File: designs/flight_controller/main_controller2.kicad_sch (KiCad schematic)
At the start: 74 parts, among them J1 xt30, J10 Conn_01x15, J3 xt30, J4 Conn_01x02, J6 Conn_01x02, J7 Conn_01x02, J8 Conn_01x02, J9 Conn_01x16, Q1 FDN359BN, SW1 SW_SPST, SW2 SW_SPST, U1 ESP32-PICO-D4, U10 BTN7030-1EPA, U11 PCA9557PW, U12 INA219AxD, U13 W25N02KVZEIR, U14 MCP2517FD-xSL, U15 SN65HVD230, U2 BMI088, U3 china_buck_converter, U4 AP7361-33ER-13, U5 MS5611-01BA, U6 BTS70802, U7 BTN7030-1EPA, U8 BTN7030-1EPA, U9 BTN7030-1EPA, Y1 40MHz

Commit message: fix grid
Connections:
- net PYRO_1_EN is gone; now on net PYRO_1: U7.6 (IN)
- net PYRO_2_EN is gone; now on net PYRO_2: U9.6 (IN)
- net PYRO_3_EN is gone; now on net PYRO_3: U8.6 (IN)
- net PYRO_4_EN is gone; now on net PYRO_4: U10.6 (IN)
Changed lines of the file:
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@@
   (no_connect (at 388.62 43.18))
   (no_connect (at 115.57 158.75))
-  (no_connect (at 130.6576 50.9016))
+  (no_connect (at 130.81 50.8))
   (no_connect (at 322.58 226.06))
   (no_connect (at 322.58 228.6))
@@
   (no_connect (at 322.58 218.44))
   (no_connect (at 243.84 151.13))
-  (no_connect (at 130.9624 48.3108))
+  (no_connect (at 130.81 48.26))
   (no_connect (at 213.995 90.17))
   (no_connect (at 213.995 82.55))
   (no_connect (at 243.84 158.75))
   (no_connect (at 64.77 234.95))
-  (no_connect (at 130.6576 45.9232))
+  (no_connect (at 130.81 45.72))
   (no_connect (at 370.84 80.01))
   (no_connect (at 353.06 38.1))
@@
     (effects (font (size 1.27 1.27)) (justify left bottom))
   )
-  (label "PYRO_3_EN" (at 74.93 262.89 180)
+  (label "PYRO_3" (at 74.93 262.89 180)
     (effects (font (size 1.27 1.27)) (justify right bottom))
   )
@@
     (effects (font (size 1.27 1.27)) (justify right bottom))
   )
-  (label "PYRO_1_EN" (at 74.93 232.41 180)
+  (label "PYRO_1" (at 74.93 232.41 180)
     (effects (font (size 1.27 1.27)) (justify right bottom))
   )
@@
     (effects (font (size 1.27 1.27)) (justify left bottom))
   )
-  (label "PYRO_4_EN" (at 139.7 264.16 180)
+  (label "PYRO_4" (at 139.7 264.16 180)
     (effects (font (size 1.27 1.27)) (justify right bottom))
   )
@@
     (effects (font (size 1.27 1.27)) (justify right bottom))
   )
-  (label "PYRO_2_EN" (at 139.7 232.41 180)
-    (effects (font (size 1.27 1.27)) (justify right bottom))
-  )
+  (label "PYRO_2" (at 139.7 232.41 180)
+    (effects (font (size 1.27 1.27)) (justify right bottom))
+  )

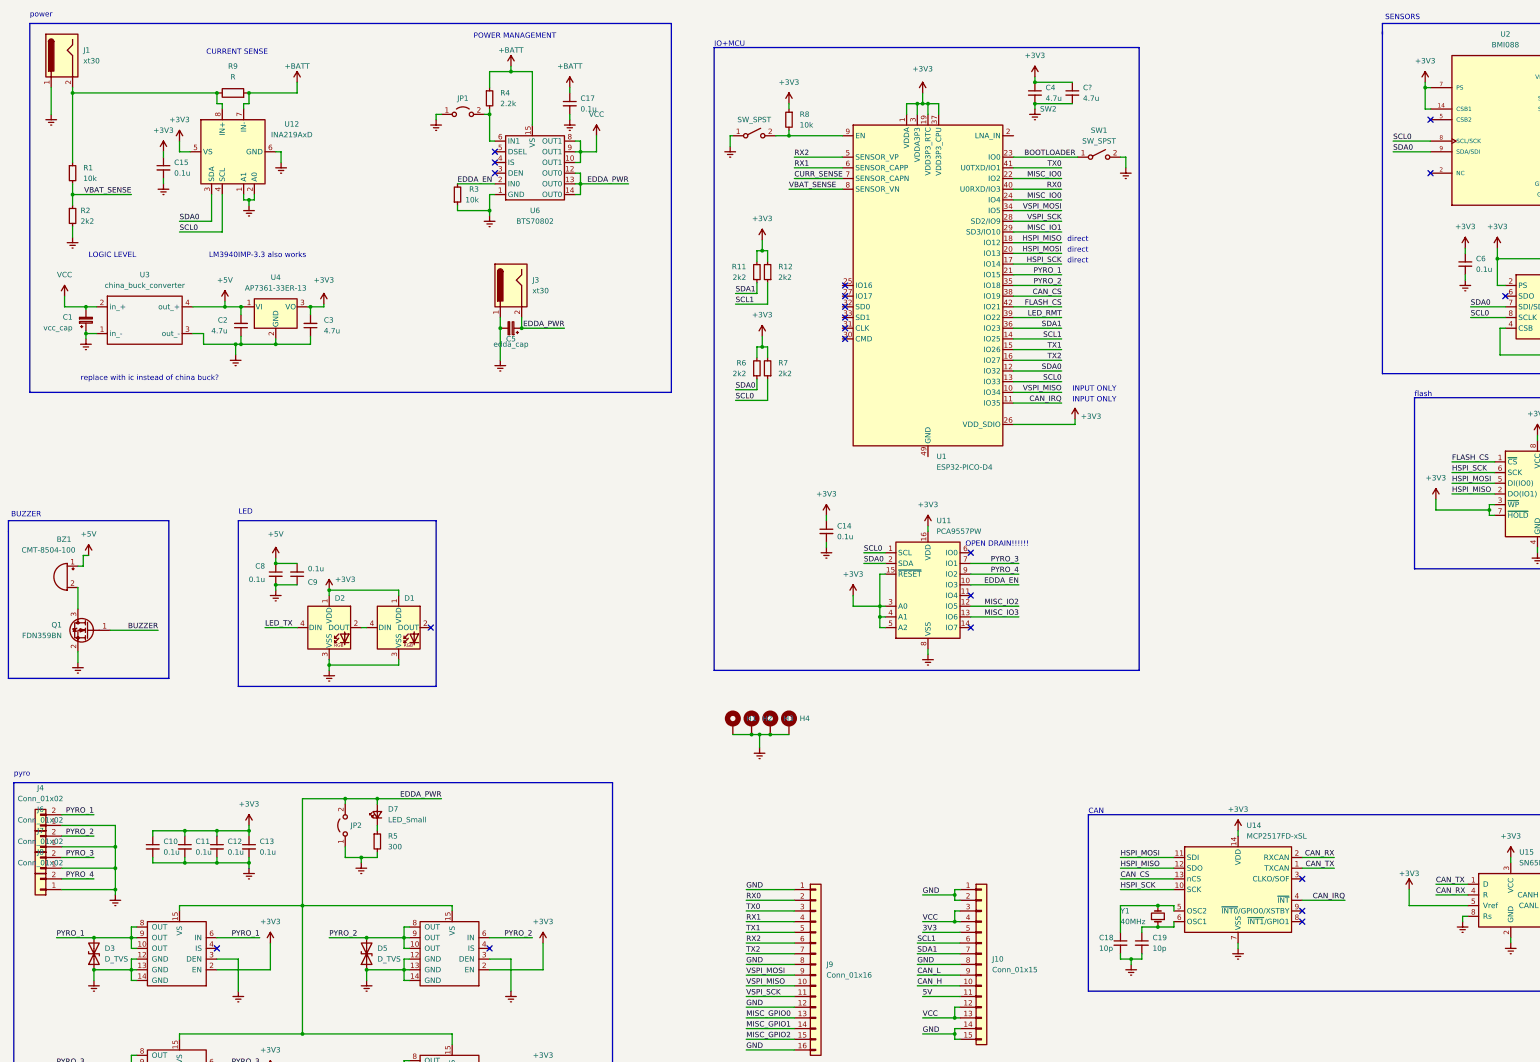
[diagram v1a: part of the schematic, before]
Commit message: preliminary layout
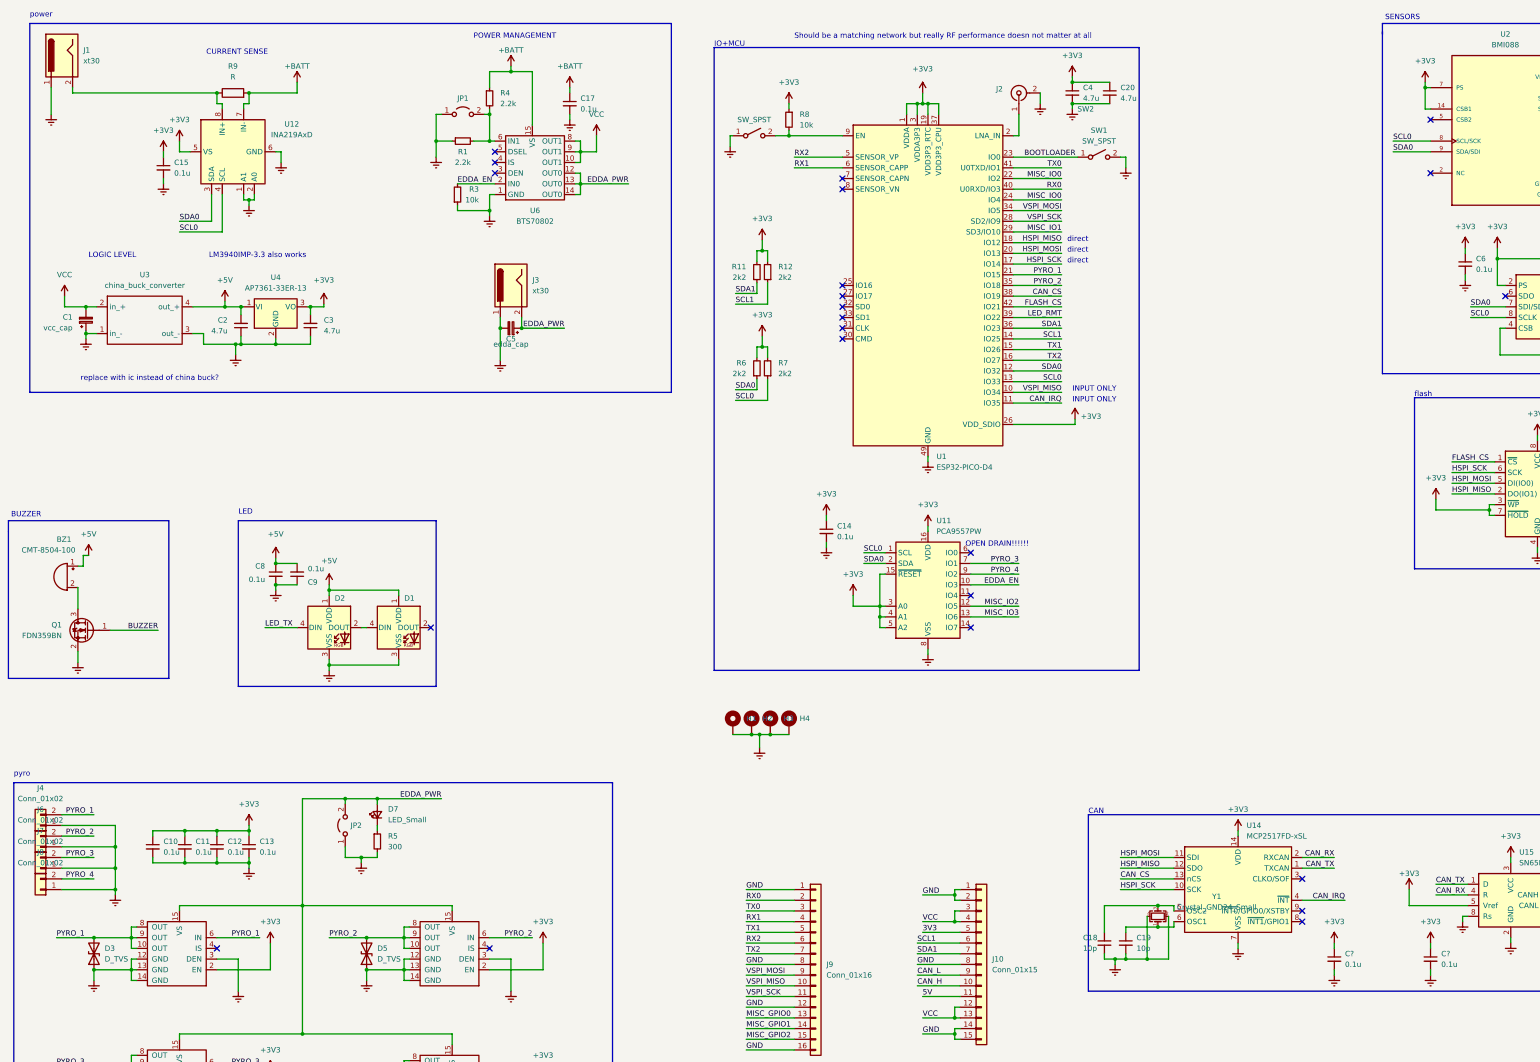
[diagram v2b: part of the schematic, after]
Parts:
- removed R2: 2k2, Resistor_SMD:R_0603_1608Metric, symbol Device:R_Small
- removed Y1: 40MHz, Oscillator:Oscillator_SMD_SeikoEpson_SG8002CE-4Pin_3.2x2.5mm_HandSoldering, symbol Device:Crystal_Small
- added C? (x2): 0.1u, Capacitor_SMD:C_0603_1608Metric, symbol Device:C_Small
- added J2: Conn_Coaxial, Connector_Coaxial:U.FL_Molex_MCRF_73412-0110_Vertical, symbol Connector:Conn_Coaxial
- added Y1: Crystal_GND24_Small, lib:CX3225SB40000D0FLJCC, symbol Device:Crystal_GND24_Small
- R1: value 10k -> 2.2k
- gave numbers to parts that had none: 1
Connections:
- net +3V3: now also C?.1, C?.1; no longer D1.1 (VDD), D2.1 (VDD)
- net +5V: now also D1.1 (VDD), D2.1 (VDD)
- net Earth: now also R1.1, U1.49 (GND), C?.2, C?.2, J2.2 (Ext), Y1.2, Y1.4
- net at JP1.2 (B), R4.2, U6.6 (IN1): now also R1.2
- net at J1.2, R9.1, U12.8 (IN+): no longer R1.1
- net at C18.1, U14.5 (OSC2): now also Y1.3
- net at C19.1, U14.6 (OSC1): now also Y1.1
- net at U1.2 (LNA_IN): now also J2.1 (In)
- net CURR_SENSE: no longer names the net of U1.7 (SENSOR_CAPN)
- net VBAT_SENSE: no longer names the net of U1.8 (SENSOR_VN)
- net VBAT_SENSE: no longer R1.2
- no-connect marks 25 -> 27
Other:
- note added: "Should be a matching network but really RF performance doesn not matter at all"
- moved on the sheet: C18, C19, C20, C4

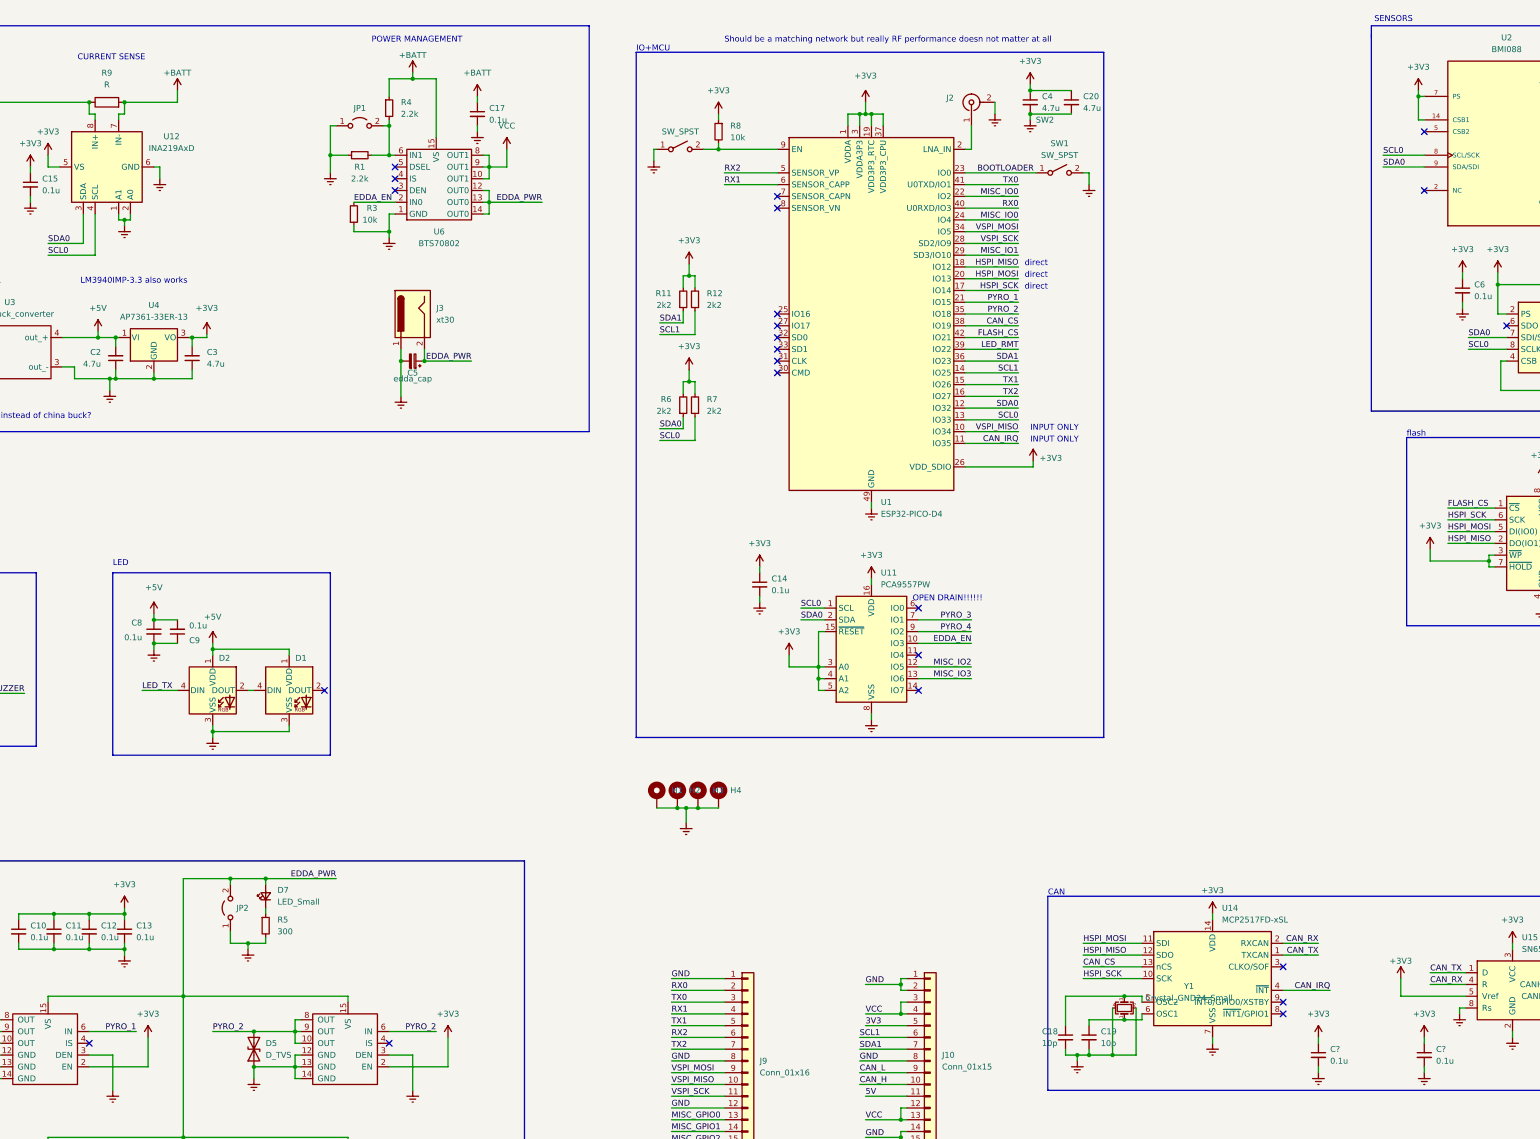
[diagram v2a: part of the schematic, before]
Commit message: add ufl
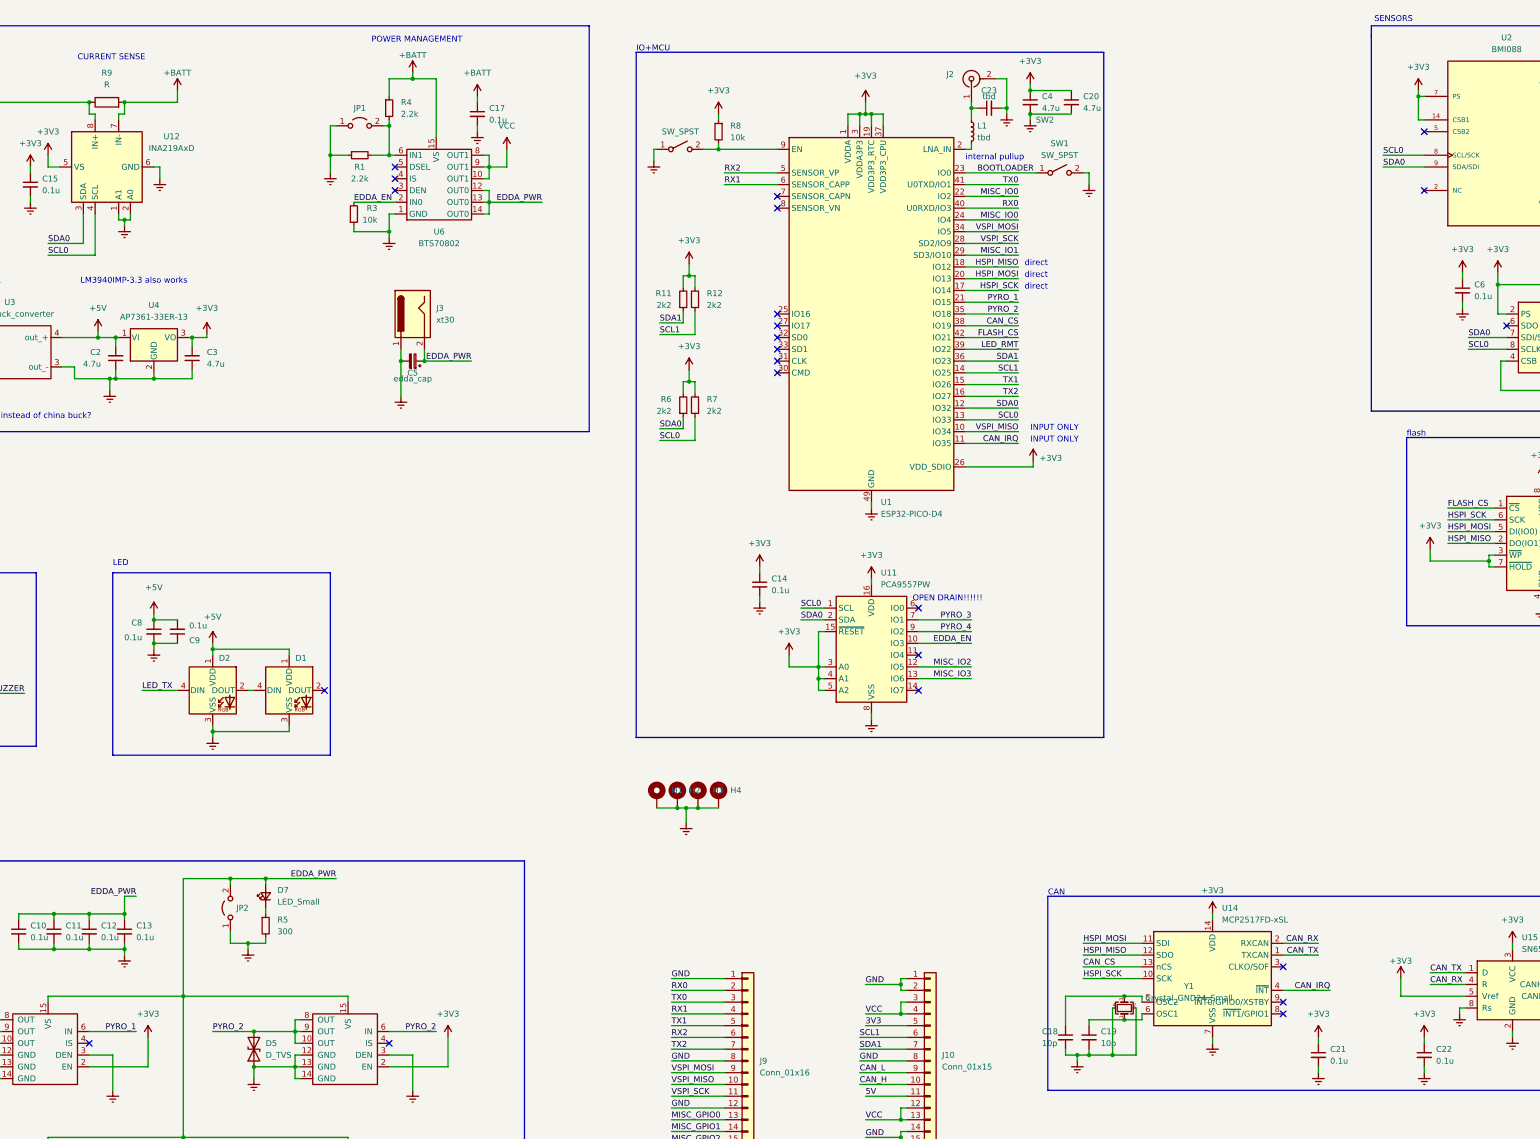
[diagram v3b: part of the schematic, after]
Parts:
- added C23: tbd, Capacitor_SMD:C_0603_1608Metric, symbol Device:C_Small
- added L1: tbd, Inductor_SMD:L_0603_1608Metric, symbol Device:L_Small
- gave numbers to parts that had none: 2
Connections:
- net +3V3: no longer C10.1, C11.1, C12.1, C13.1
- net EDDA_PWR: now also C10.1, C11.1, C12.1, C13.1
- net Earth: now also C23.2
- net at J2.1 (In): now also C23.1, L1.1; no longer U1.2 (LNA_IN)
- new net: L1.2, U1.2 (LNA_IN)
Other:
- note added: "internal pullup"
- note removed: "Should be a matching network but really RF performance doesn not matter at all"
- moved on the sheet: J2

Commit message: routing done
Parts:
- added F1: Fuse_Small, Fuse:Fuse_1812_4532Metric_Pad1.30x3.40mm_HandSolder, symbol Device:Fuse_Small
- added R13: 10k, Resistor_SMD:R_0603_1608Metric, symbol Device:R_Small
- added R14, R2: 2k2, Resistor_SMD:R_0603_1608Metric, symbol Device:R_Small
- R4: value 2.2k -> 4k7
- Y1: value Crystal_GND24_Small -> CX3225SB40000D0FLJCC
- renumbered D2 to D1, D1 to D2
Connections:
- net 3V3 is gone; now on net +5V: J10.5 (Pin_5)
- net 5V is gone; now on net +3V3: J10.11 (Pin_11)
- net LED_TX is gone; now on net LED_RMT: D1.4 (DIN)
- net MISC_GPIO0 is gone; now on net MISC_IO0: J9.13 (Pin_13)
- net MISC_GPIO1 is gone; now on net MISC_IO1: J9.14 (Pin_14)
- net MISC_GPIO2 is gone; now on net MISC_IO2: J9.15 (Pin_15)
- net +BATT: now also R2.1
- net BUZZER: now also U1.24 (IO4)
- net EDDA_PWR: now also J10.12 (Pin_12), J10.13 (Pin_13), J10.3 (Pin_3), J10.4 (Pin_4), F1.2, R13.1, R2.2; no longer U6.12 (OUT0), U6.13 (OUT0), U6.14 (OUT0)
- net Earth: now also J10.1 (Pin_1), J10.14 (Pin_14), J10.15 (Pin_15), J10.2 (Pin_2), J9.1 (Pin_1), J9.12 (Pin_12), J9.16 (Pin_16), J9.8 (Pin_8), R14.2
- net GND: no longer J10.1 (Pin_1), J10.14 (Pin_14), J10.15 (Pin_15), J10.2 (Pin_2), J9.1 (Pin_1), J9.12 (Pin_12), J9.16 (Pin_16), J9.8 (Pin_8)
- net MISC_IO0: now also U1.35 (IO18); no longer U1.22 (IO2), U1.24 (IO4)
- net PYRO_1: no longer U1.21 (IO15), U7.6 (IN)
- net PYRO_2: no longer U1.35 (IO18), U9.6 (IN)
- net PYRO_3: no longer U11.7 (IO1), U8.6 (IN)
- net PYRO_4: no longer U10.6 (IN), U11.9 (IO2)
- net RX1: now also U1.7 (SENSOR_CAPN); no longer U1.6 (SENSOR_CAPP)
- net VCC: no longer J10.12 (Pin_12), J10.13 (Pin_13), J10.3 (Pin_3), J10.4 (Pin_4)
- net SHORT_SENSE: now reaches U1.8 (SENSOR_VN)
- net SHORT_SENSE: now also R13.2, R14.1
- net MISC_IO3: no longer names the net of U11.13 (IO6)
- new net: F1.1, U6.12 (OUT0), U6.13 (OUT0), U6.14 (OUT0)
- new net PYRO_1_EN: U1.22 (IO2), U7.6 (IN)
- new net PYRO_2_EN: U1.21 (IO15), U9.6 (IN)
- new net PYRO_3_EN: U11.7 (IO1), U8.6 (IN)
- new net PYRO_4_EN: U10.6 (IN), U11.9 (IO2)
- no-connect marks 27 -> 25

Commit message: final design
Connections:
- net +3V3: no longer U15.5 (Vref)
- net Earth: now also C1.2; no longer C1.1
- net VCC: now also C1.1; no longer C1.2
- no-connect marks 25 -> 27
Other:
- note added: "check voltage"
- moved on the sheet: BZ1, Q1
